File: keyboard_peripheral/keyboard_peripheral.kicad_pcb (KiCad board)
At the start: 2 copper layers, 90.5 x 85.7 mm, 46 parts, among them IC1 ATMEGA32U4-AU, J1 USB, J2 ISP, SW17 Reset, Y1 ABM3-16.000MHZ-D2Y-T

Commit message: Updates
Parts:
- added M3-1: MountingHole_3.2mm_M3, MountingHole:MountingHole_3.2mm_M3, F.Cu at (140.7, 99.2)
- added M3-2: MountingHole_3.2mm_M3, MountingHole:MountingHole_3.2mm_M3, F.Cu at (141.1, 42.8)
- C4: moved to F.Cu
- SW17: footprint Button_Switch_SMD:SW_MEC_5GSH9 -> Button_Switch_THT:SW_PUSH_6mm_H4.3mm
- moved J2 8.93 mm to (142.0, 89.7)
- moved SW17 7.39 mm to (136.1, 25.4)
- moved C4 7.34 mm to (136.1, 35.1), turned to 90 degrees
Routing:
- net GND: track 184.0 -> 0.00 mm, vias 5 -> 0
- net ROW1: track 93.9 -> 120.7 mm, vias 0 -> 6
- net Net-(IC1-XTAL1): track 21.0 -> 13.6 mm, vias 0 -> 2
- net ROW2: track 94.8 -> 88.2 mm, vias 6 -> 3
- net ROW4: track 89.0 -> 93.3 mm
- net COL1: track 94.8 -> 99.1 mm
- net COL3: track 73.6 -> 69.7 mm
- net Net-(IC1-D+): track 38.7 -> 35.6 mm
- net Net-(C4-Pad2): track 7.98 -> 10.7 mm, vias 1 -> 0
- net Net-(J1-DP1): track 6.88 -> 4.55 mm
- net Net-(IC1-(PDO/PCINT3/MISO)_PB3): track 61.1 -> 59.2 mm
- net Net-(IC1-(PCINT1/SCLK)_PB1): track 58.7 -> 57.0 mm
- net ROW3: track 64.4 -> 66.1 mm
- net Net-(IC1-(PDI/PCINT2/MOSI)_PB2): track 59.5 -> 57.8 mm, vias 1 -> 2
- net +5V: track 120.5 -> 118.8 mm
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- added copper zone on B.Cu, net GND
- added copper zone on F.Cu, net GND
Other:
- board size 90.5 x 85.7 mm -> 89.5 x 85.7 mm
- board text added: "keypad peripheral rev 1"

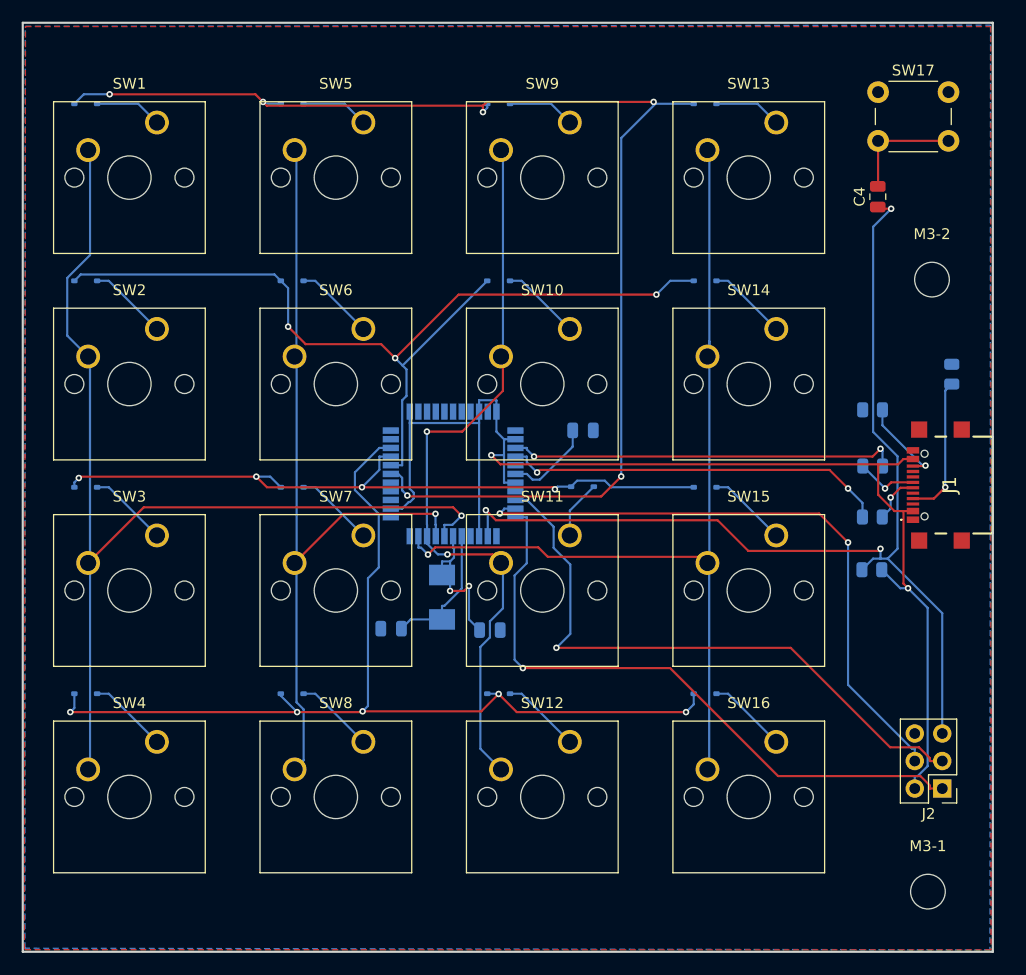
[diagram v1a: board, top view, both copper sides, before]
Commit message: Add LED; Unroute
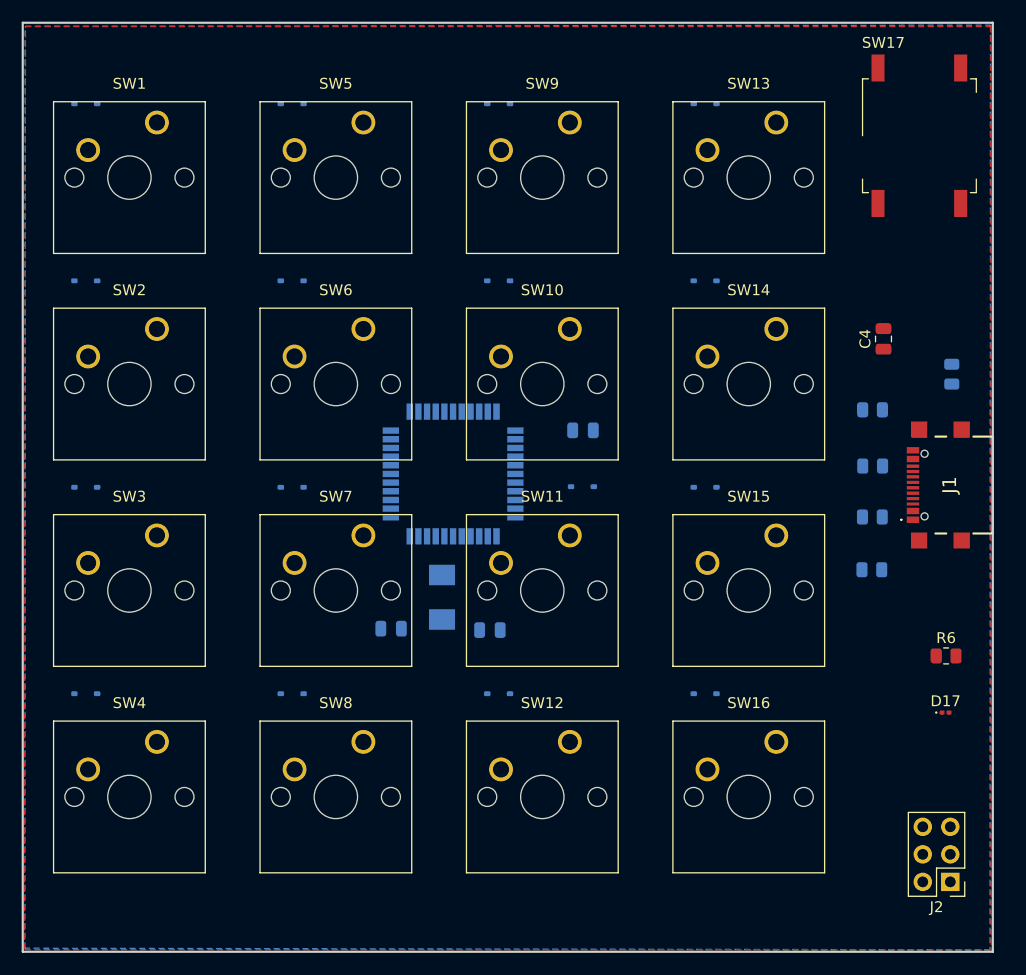
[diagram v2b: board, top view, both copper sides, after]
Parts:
- removed M3-1, M3-2: MountingHole_3.2mm_M3, MountingHole:MountingHole_3.2mm_M3
- added D17: POWER, LED_SMD:LED_0201_0603Metric, F.Cu at (142.3, 82.7)
- added R6: 330, Resistor_SMD:R_0805_2012Metric, F.Cu at (142.3, 77.5)
- C2, C3: value 22uf -> 22pf
- SW17: footprint Button_Switch_THT:SW_PUSH_6mm_H4.3mm -> Button_Switch_SMD:SW_MEC_5GSH9
- moved C4 13.1 mm to (136.6, 48.2)
- moved J2 8.64 mm to (142.7, 98.3)
- moved SW17 5.55 mm to (139.9, 29.5)
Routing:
- net ROW1: track 120.7 -> 0.00 mm, vias 6 -> 0
- net +5V: track 118.8 -> 0.00 mm, vias 2 -> 0
- net COL1: track 99.1 -> 0.00 mm, vias 1 -> 0
- net Net-(IC1-~{RESET}): track 98.0 -> 0.00 mm, vias 3 -> 0
- net ROW4: track 93.3 -> 0.00 mm, vias 5 -> 0
- net ROW2: track 88.2 -> 0.00 mm, vias 3 -> 0
- net COL4: track 87.8 -> 0.00 mm, vias 1 -> 0
- net COL2: track 75.1 -> 0.00 mm, vias 1 -> 0
- net COL3: track 69.7 -> 0.00 mm, vias 2 -> 0
- net ROW3: track 66.1 -> 0.00 mm, vias 4 -> 0
- net Net-(IC1-(PDO/PCINT3/MISO)_PB3): track 59.2 -> 0.00 mm, vias 1 -> 0
- net Net-(IC1-(PDI/PCINT2/MOSI)_PB2): track 57.8 -> 0.00 mm, vias 2 -> 0
- net Net-(IC1-(PCINT1/SCLK)_PB1): track 57.0 -> 0.00 mm, vias 1 -> 0
- net Net-(IC1-D-): track 36.1 -> 0.00 mm, vias 2 -> 0
- net Net-(IC1-D+): track 35.6 -> 0.00 mm, vias 2 -> 0
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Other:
- board text added: "keypad peripheral rev 2"
- board text removed: "keypad peripheral rev 1"

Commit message: rerouting
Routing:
- net GND: track 0.00 -> 213.6 mm, vias 0 -> 14
- net +5V: track 0.00 -> 132.1 mm, vias 0 -> 4
- net ROW2: track 0.00 -> 100.4 mm, vias 0 -> 6
- net COL1: track 0.00 -> 97.8 mm, vias 0 -> 1
- net ROW1: track 0.00 -> 97.2 mm, vias 0 -> 3
- net ROW4: track 0.00 -> 92.8 mm, vias 0 -> 5
- net Net-(IC1-~{RESET}): track 0.00 -> 89.1 mm, vias 0 -> 3
- net COL4: track 0.00 -> 86.3 mm, vias 0 -> 1
- net Net-(IC1-(PDO/PCINT3/MISO)_PB3): track 0.00 -> 76.7 mm, vias 0 -> 1
- net Net-(IC1-(PCINT1/SCLK)_PB1): track 0.00 -> 75.0 mm, vias 0 -> 2
- net COL3: track 0.00 -> 74.9 mm, vias 0 -> 2
- net COL2: track 0.00 -> 73.4 mm, vias 0 -> 1
- net ROW3: track 0.00 -> 69.3 mm, vias 0 -> 4
- net Net-(IC1-(PDI/PCINT2/MOSI)_PB2): track 0.00 -> 58.1 mm, vias 0 -> 1
- net Net-(IC1-D-): track 0.00 -> 38.6 mm, vias 0 -> 2
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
